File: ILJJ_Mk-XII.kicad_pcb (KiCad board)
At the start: 2 copper layers, 13 parts, among them SW0 SW_SPDT, SW1 SW_SPDT, SW2 SW_SPDT

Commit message: 外形、ネジ穴、GNDベタを追加
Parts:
- added REF**: MountingHole_3.2mm_M3, MountingHole:MountingHole_3.2mm_M3, F.Cu at (58.4, 51.4)
- added REF**: MountingHole_3.2mm_M3, MountingHole:MountingHole_3.2mm_M3, F.Cu at (58.4, 91.4)
- added REF**: MountingHole_3.2mm_M3, MountingHole:MountingHole_3.2mm_M3, F.Cu at (114.3, 91.4)
- added REF**: MountingHole_3.2mm_M3, MountingHole:MountingHole_3.2mm_M3, F.Cu at (114.3, 51.4)
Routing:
- added copper zone on B.Cu, net GND
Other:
- board outline added: 64.1 x 47.6 mm
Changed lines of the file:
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@@
   (general
     (thickness 1.6)
-    (drawings 0)
+    (drawings 4)
     (tracks 46)
     (zones 0)
-    (modules 13)
+    (modules 17)
     (nets 24)
   )
@@
     (uvia_drill 0.1)
   )
+  (module MountingHole:MountingHole_3.2mm_M3 (layer F.Cu)
+    (at 58.42 51.435)
+    (descr "Mounting Hole 3.2mm, no annular, M3")
+    (tags "mounting hole 3.2mm no annular m3")
+    (attr virtual)
+    (fp_text reference REF** (at 0 -4.2) (layer F.SilkS)
+      (effects (font (size 1 1) (thickness 0.15)))
+    )
+    (fp_text value MountingHole_3.2mm_M3 (at 0 4.2) (layer F.Fab)
+      (effects (font (size 1 1) (thickness 0.15)))
+    )
+    (fp_circle (center 0 0) (end 3.45 0) (layer F.CrtYd) (width 0.05))
+    (fp_circle (center 0 0) (end 3.2 0) (layer Cmts.User) (width 0.15))
+    (fp_text user %R (at 0.3 0) (layer F.Fab)
+      (effects (font (size 1 1) (thickness 0.15)))
+    )
+    (pad 1 np_thru_hole circle (at 0 0) (size 3.2 3.2) (drill 3.2) (layers *.Cu *.Mask))
+  )
   (module Connector_PinHeader_2.54mm:PinHeader_2x12_P2.54mm_Vertical (layer F.Cu)
     (at 62.23 57.15)
@@
     )
   )
+  (module MountingHole:MountingHole_3.2mm_M3 (layer F.Cu)
+    (at 58.42 91.44)
+    (descr "Mounting Hole 3.2mm, no annular, M3")
+    (tags "mounting hole 3.2mm no annular m3")
+    (attr virtual)
+    (fp_text reference REF** (at 0 -4.2) (layer F.SilkS)
+      (effects (font (size 1 1) (thickness 0.15)))
+    )
+    (fp_text value MountingHole_3.2mm_M3 (at 0 4.2) (layer F.Fab)
+      (effects (font (size 1 1) (thickness 0.15)))
+    )
+    (fp_circle (center 0 0) (end 3.45 0) (layer F.CrtYd) (width 0.05))
+    (fp_circle (center 0 0) (end 3.2 0) (layer Cmts.User) (width 0.15))
+    (fp_text user %R (at 0.3 0) (layer F.Fab)
+      (effects (font (size 1 1) (thickness 0.15)))
+    )
+    (pad 1 np_thru_hole circle (at 0 0) (size 3.2 3.2) (drill 3.2) (layers *.Cu *.Mask))
+  )
+  (module MountingHole:MountingHole_3.2mm_M3 (layer F.Cu)
+    (at 114.3 91.44)
+    (descr "Mounting Hole 3.2mm, no annular, M3")
+    (tags "mounting hole 3.2mm no annular m3")
+    (attr virtual)
+    (fp_text reference REF** (at 0 -4.2) (layer F.SilkS)
+      (effects (font (size 1 1) (thickness 0.15)))
+    )
+    (fp_text value MountingHole_3.2mm_M3 (at 0 4.2) (layer F.Fab)
+      (effects (font (size 1 1) (thickness 0.15)))
+    )
+    (fp_circle (center 0 0) (end 3.45 0) (layer F.CrtYd) (width 0.05))
+    (fp_circle (center 0 0) (end 3.2 0) (layer Cmts.User) (width 0.15))
+    (fp_text user %R (at 0.3 0) (layer F.Fab)
+      (effects (font (size 1 1) (thickness 0.15)))
+    )
+    (pad 1 np_thru_hole circle (at 0 0) (size 3.2 3.2) (drill 3.2) (layers *.Cu *.Mask))
+  )
+  (module MountingHole:MountingHole_3.2mm_M3 (layer F.Cu)
+    (at 114.3 51.435)
+    (descr "Mounting Hole 3.2mm, no annular, M3")
+    (tags "mounting hole 3.2mm no annular m3")
+    (attr virtual)
+    (fp_text reference REF** (at 0 -4.2) (layer F.SilkS)
+      (effects (font (size 1 1) (thickness 0.15)))
+    )
+    (fp_text value MountingHole_3.2mm_M3 (at 0 4.2) (layer F.Fab)
+      (effects (font (size 1 1) (thickness 0.15)))
+    )
+    (fp_circle (center 0 0) (end 3.45 0) (layer F.CrtYd) (width 0.05))
+    (fp_circle (center 0 0) (end 3.2 0) (layer Cmts.User) (width 0.15))
+    (fp_text user %R (at 0.3 0) (layer F.Fab)
+      (effects (font (size 1 1) (thickness 0.15)))
+    )
+    (pad 1 np_thru_hole circle (at 0 0) (size 3.2 3.2) (drill 3.2) (layers *.Cu *.Mask))
+  )
+  (gr_line (start 118.11 47.625) (end 53.975 47.625) (layer Edge.Cuts) (width 0.15))
+  (gr_line (start 118.11 95.25) (end 118.11 47.625) (layer Edge.Cuts) (width 0.15))
+  (gr_line (start 53.975 95.25) (end 118.11 95.25) (layer Edge.Cuts) (width 0.15))
+  (gr_line (start 53.975 47.625) (end 53.975 95.25) (layer Edge.Cuts) (width 0.15))
   (segment (start 62.23 57.15) (end 64.77 57.15) (width 1) (layer B.Cu) (net 1))
   (segment (start 69.85 52.07) (end 108.585 52.07) (width 1) (layer B.Cu) (net 1))
@@
     (connect_pads (clearance 0.508))
     (min_thickness 0.254)
-    (keepout (tracks not_allowed) (vias not_allowed) (copperpour allowed))
+    (keepout (tracks not_allowed) (vias not_allowed) (copperpour not_allowed))
     (fill (arc_segments 16) (thermal_gap 0.508) (thermal_bridge_width 0.508))
     (polygon
@@
       )
     )
+  )
+  (zone (net 5) (net_name GND) (layer B.Cu) (hatch edge 0.508)
+    (connect_pads (clearance 0.508))
+    (min_thickness 0.254)
+    (fill yes (arc_segments 16) (thermal_gap 0.508) (thermal_bridge_width 0.508))
+    (polygon
+      (pts
+        (xy 118.11 47.625) (xy 118.11 95.25) (xy 53.975 95.25) (xy 53.975 47.625)
+      )
+    )

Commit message: [fix] 基板外形や配線の修正
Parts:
- moved REF** 3.81 mm to (62.2, 51.4)
- moved REF** 3.81 mm to (62.2, 91.4)
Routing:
- net /F0: track 76.6 -> 71.2 mm
- net /F1: track 62.4 -> 58.0 mm
- net /F2: track 47.5 -> 49.3 mm
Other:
- board size 64.1 x 47.6 mm -> 59.7 x 47.6 mm
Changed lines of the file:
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@@
-(kicad_pcb (version 20171130) (host pcbnew "(5.0.0)")
+(kicad_pcb (version 20171130) (host pcbnew "(5.0.0-3-g5ebb6b6)")
   (general
     (thickness 1.6)
     (drawings 4)
-    (tracks 46)
+    (tracks 39)
     (zones 0)
     (modules 17)
@@
   )
   (module MountingHole:MountingHole_3.2mm_M3 (layer F.Cu)
-    (at 58.42 51.435)
+    (at 62.23 51.435)
     (descr "Mounting Hole 3.2mm, no annular, M3")
     (tags "mounting hole 3.2mm no annular m3")
@@
   )
   (module MountingHole:MountingHole_3.2mm_M3 (layer F.Cu)
-    (at 58.42 91.44)
+    (at 62.23 91.44)
     (descr "Mounting Hole 3.2mm, no annular, M3")
     (tags "mounting hole 3.2mm no annular m3")
@@
     (pad 1 np_thru_hole circle (at 0 0) (size 3.2 3.2) (drill 3.2) (layers *.Cu *.Mask))
   )
-  (gr_line (start 118.11 47.625) (end 53.975 47.625) (layer Edge.Cuts) (width 0.15))
+  (gr_line (start 118.11 47.625) (end 58.42 47.625) (layer Edge.Cuts) (width 0.15))
   (gr_line (start 118.11 95.25) (end 118.11 47.625) (layer Edge.Cuts) (width 0.15))
-  (gr_line (start 53.975 95.25) (end 118.11 95.25) (layer Edge.Cuts) (width 0.15))
-  (gr_line (start 53.975 47.625) (end 53.975 95.25) (layer Edge.Cuts) (width 0.15))
+  (gr_line (start 58.42 95.25) (end 118.11 95.25) (layer Edge.Cuts) (width 0.15))
+  (gr_line (start 58.42 47.625) (end 58.42 95.25) (layer Edge.Cuts) (width 0.15))
   (segment (start 62.23 57.15) (end 64.77 57.15) (width 1) (layer B.Cu) (net 1))
   (segment (start 69.85 52.07) (end 108.585 52.07) (width 1) (layer B.Cu) (net 1))
@@
   (segment (start 96.52 85.09) (end 102.87 85.09) (width 1) (layer B.Cu) (net 1))
   (segment (start 102.87 85.09) (end 112.395 75.565) (width 1) (layer B.Cu) (net 1))
+  (segment (start 64.77 80.01) (end 62.23 80.01) (width 1) (layer B.Cu) (net 2))
+  (segment (start 66.675 64.77) (end 64.77 64.77) (width 1) (layer B.Cu) (net 2))
   (segment (start 73.66 64.77) (end 62.23 64.77) (width 1) (layer B.Cu) (net 2))
-  (segment (start 64.77 80.01) (end 62.23 80.01) (width 1) (layer B.Cu) (net 2))
-  (segment (start 72.760001 74.030001) (end 69.85 71.12) (width 1) (layer B.Cu) (net 2))
-  (segment (start 73.66 74.93) (end 72.760001 74.030001) (width 1) (layer B.Cu) (net 2))
-  (segment (start 73.66 64.77) (end 78.74 59.69) (width 1) (layer B.Cu) (net 2))
-  (segment (start 66.675 64.77) (end 64.77 64.77) (width 1) (layer B.Cu) (net 2))
-  (segment (start 69.215 67.31) (end 66.675 64.77) (width 1) (layer B.Cu) (net 2))
-  (segment (start 69.85 71.12) (end 69.215 70.485) (width 1) (layer B.Cu) (net 2))
-  (segment (start 69.215 70.485) (end 69.215 67.31) (width 1) (layer B.Cu) (net 2))
-  (segment (start 69.215 71.755) (end 69.215 70.485) (width 1) (layer B.Cu) (net 2))
-  (segment (start 64.77 80.01) (end 69.215 75.565) (width 1) (layer B.Cu) (net 2))
-  (segment (start 69.215 75.565) (end 69.215 71.755) (width 1) (layer B.Cu) (net 2))
+  (segment (start 73.66 74.93) (end 78.74 69.85) (width 1) (layer B.Cu) (net 2))
+  (segment (start 66.04 80.01) (end 64.77 80.01) (width 1) (layer B.Cu) (net 2))
+  (segment (start 71.12 74.93) (end 66.04 80.01) (width 1) (layer B.Cu) (net 2))
+  (segment (start 73.66 74.93) (end 71.12 74.93) (width 1) (layer B.Cu) (net 2))
+  (segment (start 73.66 64.77) (end 78.74 64.77) (width 1) (layer B.Cu) (net 2))
+  (segment (start 78.74 64.77) (end 78.74 59.69) (width 1) (layer B.Cu) (net 2))
+  (segment (start 78.74 69.85) (end 78.74 64.77) (width 1) (layer B.Cu) (net 2))
   (segment (start 64.77 62.23) (end 62.23 62.23) (width 1) (layer B.Cu) (net 3))
   (segment (start 65.619999 61.380001) (end 64.77 62.23) (width 1) (layer B.Cu) (net 3))
@@
   (segment (start 88.9 55.88) (end 92.71 59.69) (width 1) (layer B.Cu) (net 3))
   (segment (start 79.375 55.88) (end 88.9 55.88) (width 1) (layer B.Cu) (net 3))
-  (segment (start 82.55 70.485) (end 86.995 74.93) (width 1) (layer B.Cu) (net 3))
-  (segment (start 82.55 62.23) (end 82.55 70.485) (width 1) (layer B.Cu) (net 3))
-  (segment (start 86.995 64.77) (end 85.09 64.77) (width 1) (layer B.Cu) (net 3))
-  (segment (start 85.09 64.77) (end 82.55 62.23) (width 1) (layer B.Cu) (net 3))
-  (segment (start 82.55 59.055) (end 79.375 55.88) (width 1) (layer B.Cu) (net 3))
-  (segment (start 82.55 62.23) (end 82.55 59.055) (width 1) (layer B.Cu) (net 3))
+  (segment (start 92.71 69.215) (end 86.995 74.93) (width 1) (layer B.Cu) (net 3))
+  (segment (start 86.995 64.77) (end 92.71 64.77) (width 1) (layer B.Cu) (net 3))
+  (segment (start 92.71 64.77) (end 92.71 69.215) (width 1) (layer B.Cu) (net 3))
+  (segment (start 92.71 59.69) (end 92.71 64.77) (width 1) (layer B.Cu) (net 3))
   (segment (start 62.23 59.69) (end 64.77 59.69) (width 1) (layer B.Cu) (net 4))
   (segment (start 99.695 53.975) (end 105.41 59.69) (width 1) (layer B.Cu) (net 4))
   (segment (start 92.075 53.975) (end 99.695 53.975) (width 1) (layer B.Cu) (net 4))
-  (segment (start 99.695 64.77) (end 97.79 64.77) (width 1) (layer B.Cu) (net 4))
-  (segment (start 97.79 64.77) (end 96.52 63.5) (width 1) (layer B.Cu) (net 4))
   (segment (start 65.619999 58.840001) (end 64.77 59.69) (width 1) (layer B.Cu) (net 4))
   (segment (start 92.075 53.975) (end 70.485 53.975) (width 1) (layer B.Cu) (net 4))
   (segment (start 70.485 53.975) (end 65.619999 58.840001) (width 1) (layer B.Cu) (net 4))
-  (segment (start 95.885 57.785) (end 92.075 53.975) (width 1) (layer B.Cu) (net 4))
-  (segment (start 96.52 63.5) (end 95.885 62.865) (width 1) (layer B.Cu) (net 4))
-  (segment (start 95.885 62.865) (end 95.885 57.785) (width 1) (layer B.Cu) (net 4))
-  (segment (start 95.885 71.12) (end 99.695 74.93) (width 1) (layer B.Cu) (net 4))
-  (segment (start 95.885 62.865) (end 95.885 71.12) (width 1) (layer B.Cu) (net 4))
+  (segment (start 105.41 69.215) (end 99.695 74.93) (width 1) (layer B.Cu) (net 4))
+  (segment (start 105.41 64.77) (end 105.41 69.215) (width 1) (layer B.Cu) (net 4))
+  (segment (start 99.695 64.77) (end 105.41 64.77) (width 1) (layer B.Cu) (net 4))
+  (segment (start 105.41 59.69) (end 105.41 64.77) (width 1) (layer B.Cu) (net 4))
   (segment (start 108.585 59.69) (end 108.585 64.77) (width 1) (layer B.Cu) (net 20))
   (zone (net 0) (net_name "") (layer B.Cu) (hatch edge 0.508)
@@
     (polygon
       (pts
-        (xy 118.11 47.625) (xy 118.11 95.25) (xy 53.975 95.25) (xy 53.975 47.625)
+        (xy 118.11 47.625) (xy 118.11 95.25) (xy 58.42 95.25) (xy 58.42 47.625)
       )
     )

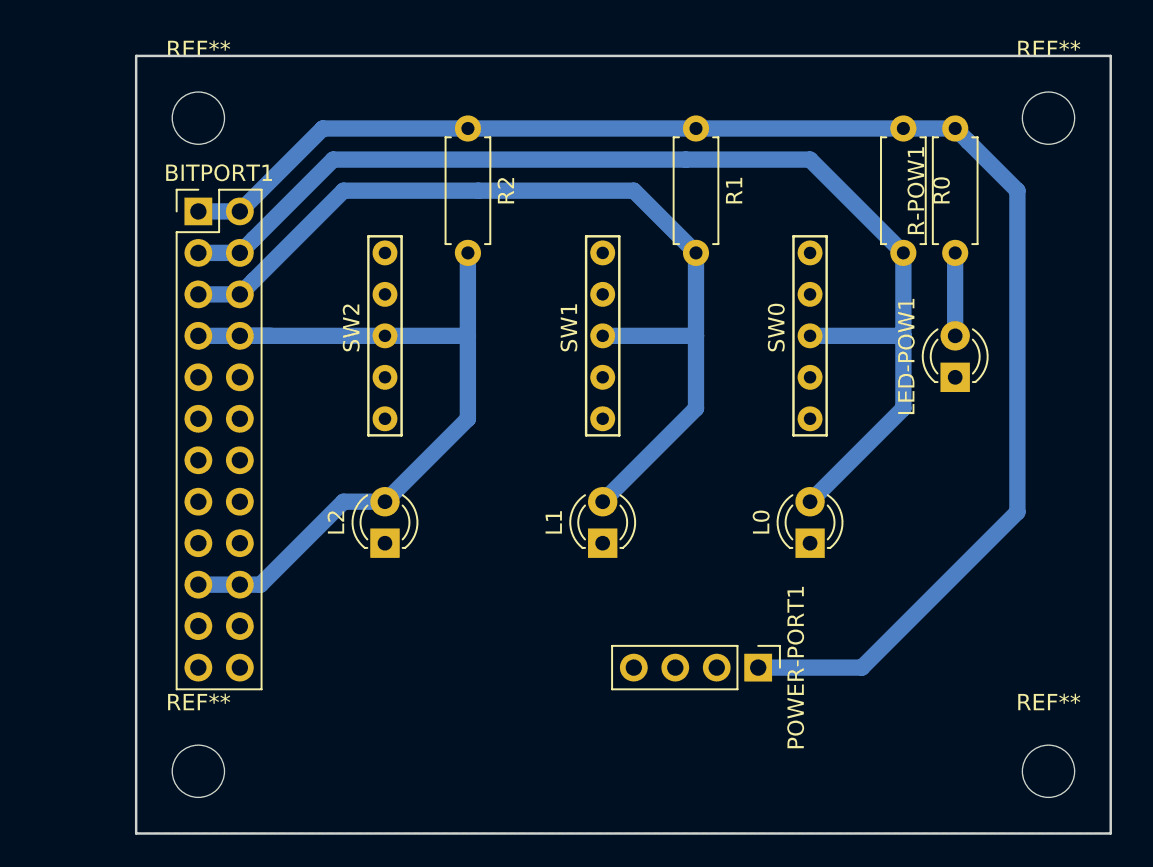
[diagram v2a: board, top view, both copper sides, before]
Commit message: 回路図の修正とGNDベタ入れ
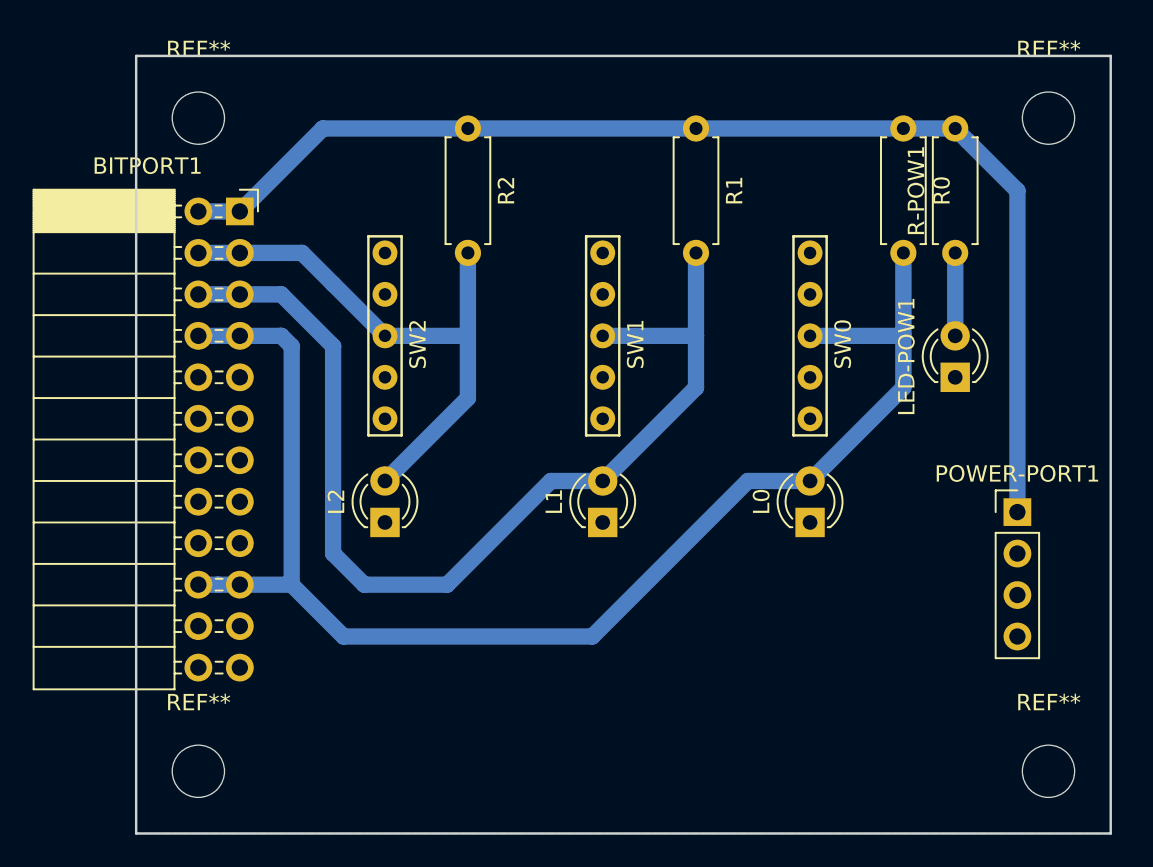
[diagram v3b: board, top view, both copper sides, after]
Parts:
- BITPORT1: footprint Connector_PinHeader_2.54mm:PinHeader_2x12_P2.54mm_Vertical -> Connector_PinSocket_2.54mm:PinSocket_2x12_P2.54mm_Horizontal
- moved POWER-PORT1 18.5 mm to (112.4, 75.6), turned to 0 degrees
- moved SW0 10.2 mm to (99.7, 59.7), turned to 270 degrees
- moved SW1 10.2 mm to (87.0, 59.7), turned to 270 degrees
- moved SW2 10.2 mm to (73.7, 59.7), turned to 270 degrees
- moved BITPORT1 2.54 mm to (64.8, 57.1)
- moved L0 1.27 mm to (99.7, 76.2)
- moved L1 1.27 mm to (87.0, 76.2)
- moved L2 1.27 mm to (73.7, 76.2)
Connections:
- BITPORT1 pad 19: /F2 -> /F0
- BITPORT1 pad 20: /F2 -> /F0
- BITPORT1 pad 3: /F0 -> /F2
- BITPORT1 pad 4: /F0 -> /F2
- BITPORT1 pad 7: /F2 -> /F0
- BITPORT1 pad 8: /F2 -> /F0
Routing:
- net +5VA: track 93.4 -> 73.5 mm
- net /F2: track 49.3 -> 34.7 mm
- net /F0: track 71.2 -> 85.4 mm
- net /F1: track 58.0 -> 64.3 mm

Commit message: update 基板(?)データ
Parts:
- removed REF** (x4): MountingHole_3.2mm_M3, MountingHole:MountingHole_3.2mm_M3
- moved R2 1.91 mm to (80.6, 52.1)
- moved L2 1.27 mm to (74.9, 76.2)
- moved SW2 1.27 mm to (74.9, 59.7)
- moved R0 1.27 mm to (104.1, 52.1)
- moved L0 0.63 mm to (99.1, 76.2)
- moved SW0 0.63 mm to (99.1, 59.7)
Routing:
- net /F2: track 34.7 -> 37.6 mm
- net /F1: track 64.3 -> 65.4 mm
- net /F0: track 85.4 -> 84.3 mm
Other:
- outline, holes or cut-outs redrawn
